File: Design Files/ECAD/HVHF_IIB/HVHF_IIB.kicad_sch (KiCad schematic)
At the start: 70 parts, among them J1 1984963, J2 1984963, J3 731375003, J4 CONSMA002-L, J5 1984963, Q1 PNP, Q2 BFP196E6327HTSA1, T1 BFU590G, T10 BFQ252, T11 BFQ252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

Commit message: fixed orientation error T4,T10-T12
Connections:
- net GND: now also T10.2 (C), T11.2 (C), T4.2 (C); no longer T10.1 (E), T11.1 (E), T12.1 (E), T4.1 (E)
- net at R21.2, T7.1 (E): now also T11.1 (E); no longer T11.2 (C)
- net at R12.2, T5.1 (E): now also T4.1 (E); no longer T4.2 (C)
- net at R22.2, T9.1 (E): now also T12.1 (E); no longer T12.2 (C)
- net at R20.2, T6.1 (E): now also T10.1 (E); no longer T10.2 (C)

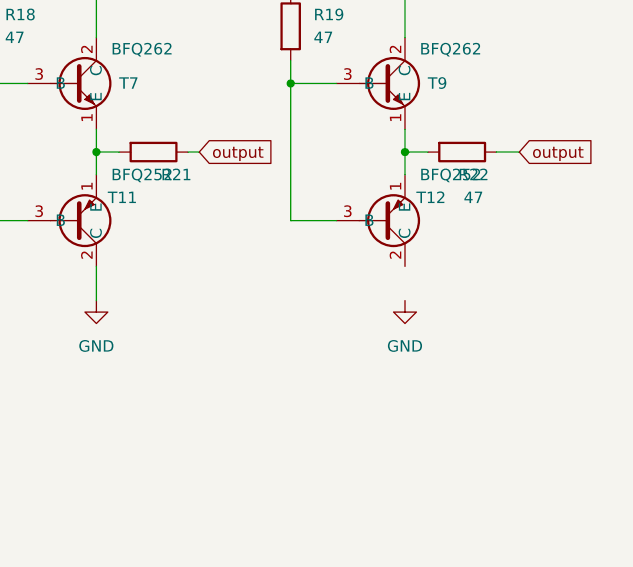
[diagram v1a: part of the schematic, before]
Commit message: fixed unconnected GND power pin
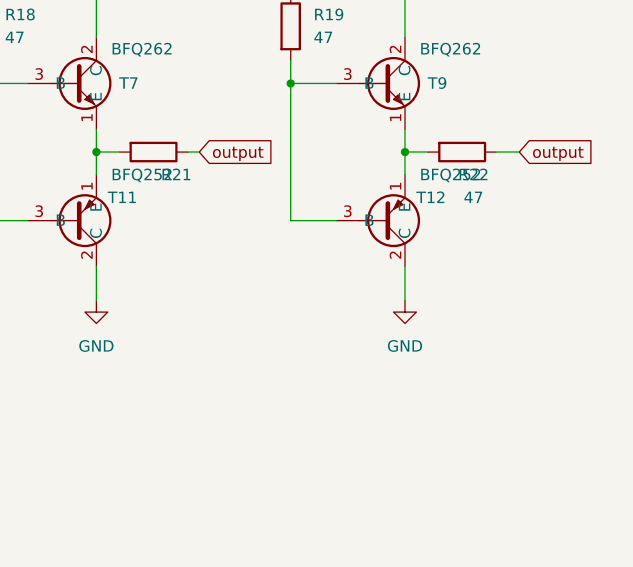
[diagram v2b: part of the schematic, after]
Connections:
- net GND: now also T12.2 (C)
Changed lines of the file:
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@@
+    (stroke (width 0) (type default))
+  )
+  (wire (pts (xy 262.89 154.94) (xy 262.89 158.75))
     (stroke (width 0) (type default))
   )

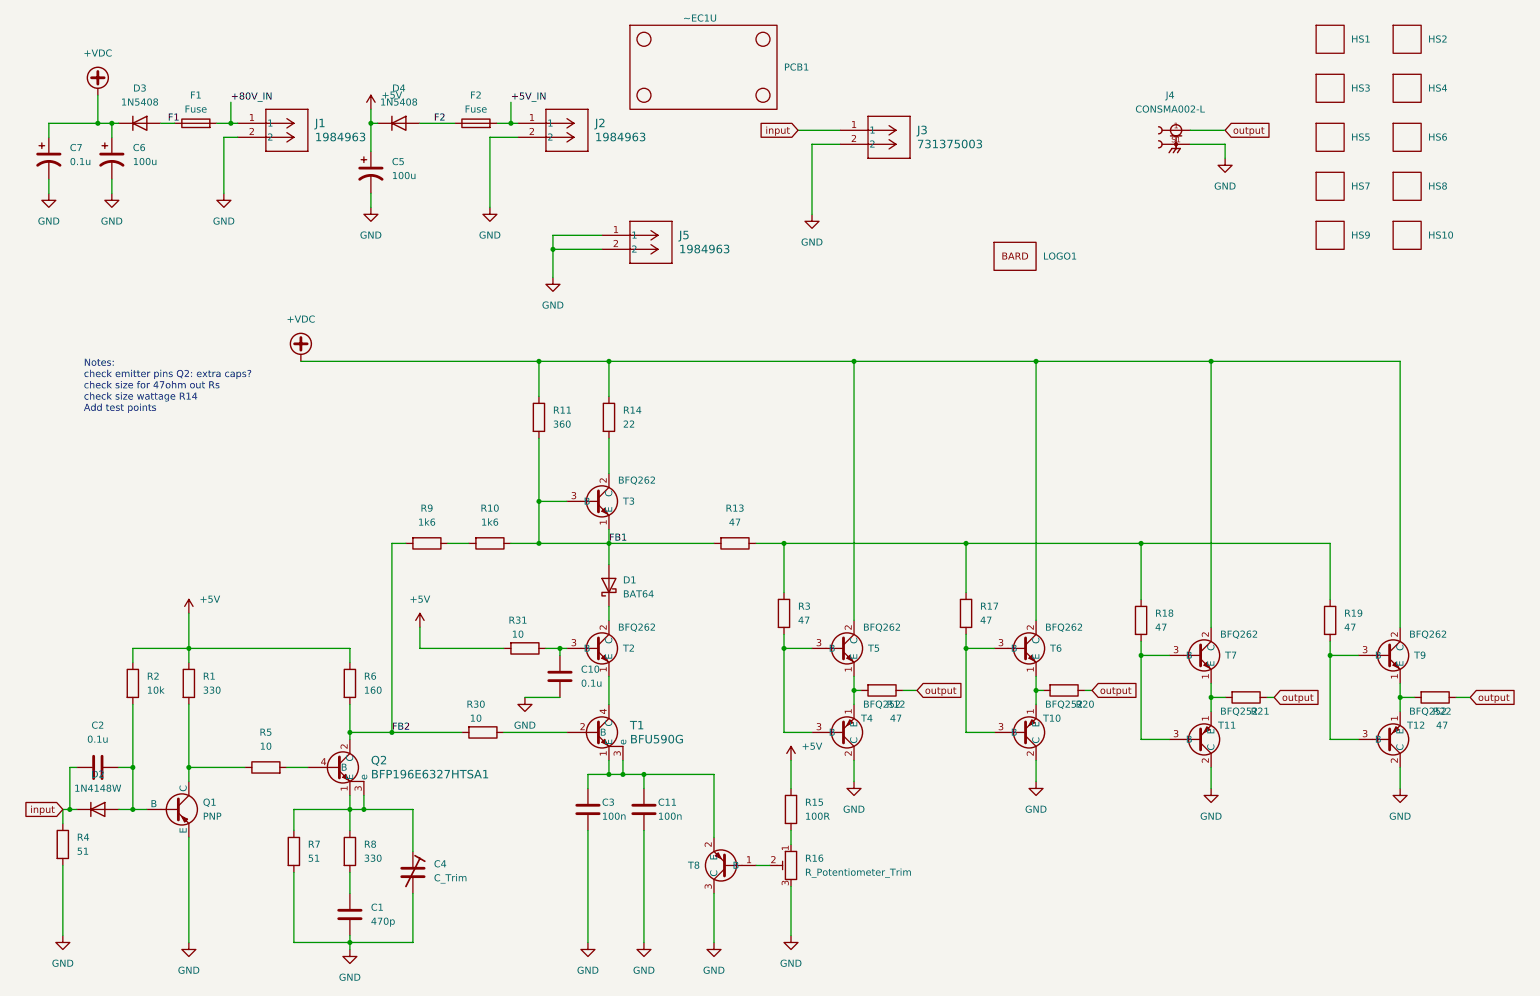
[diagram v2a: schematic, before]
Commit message: fixes, adds, silk
fixed Q1 rotation
adds LED
adds GND
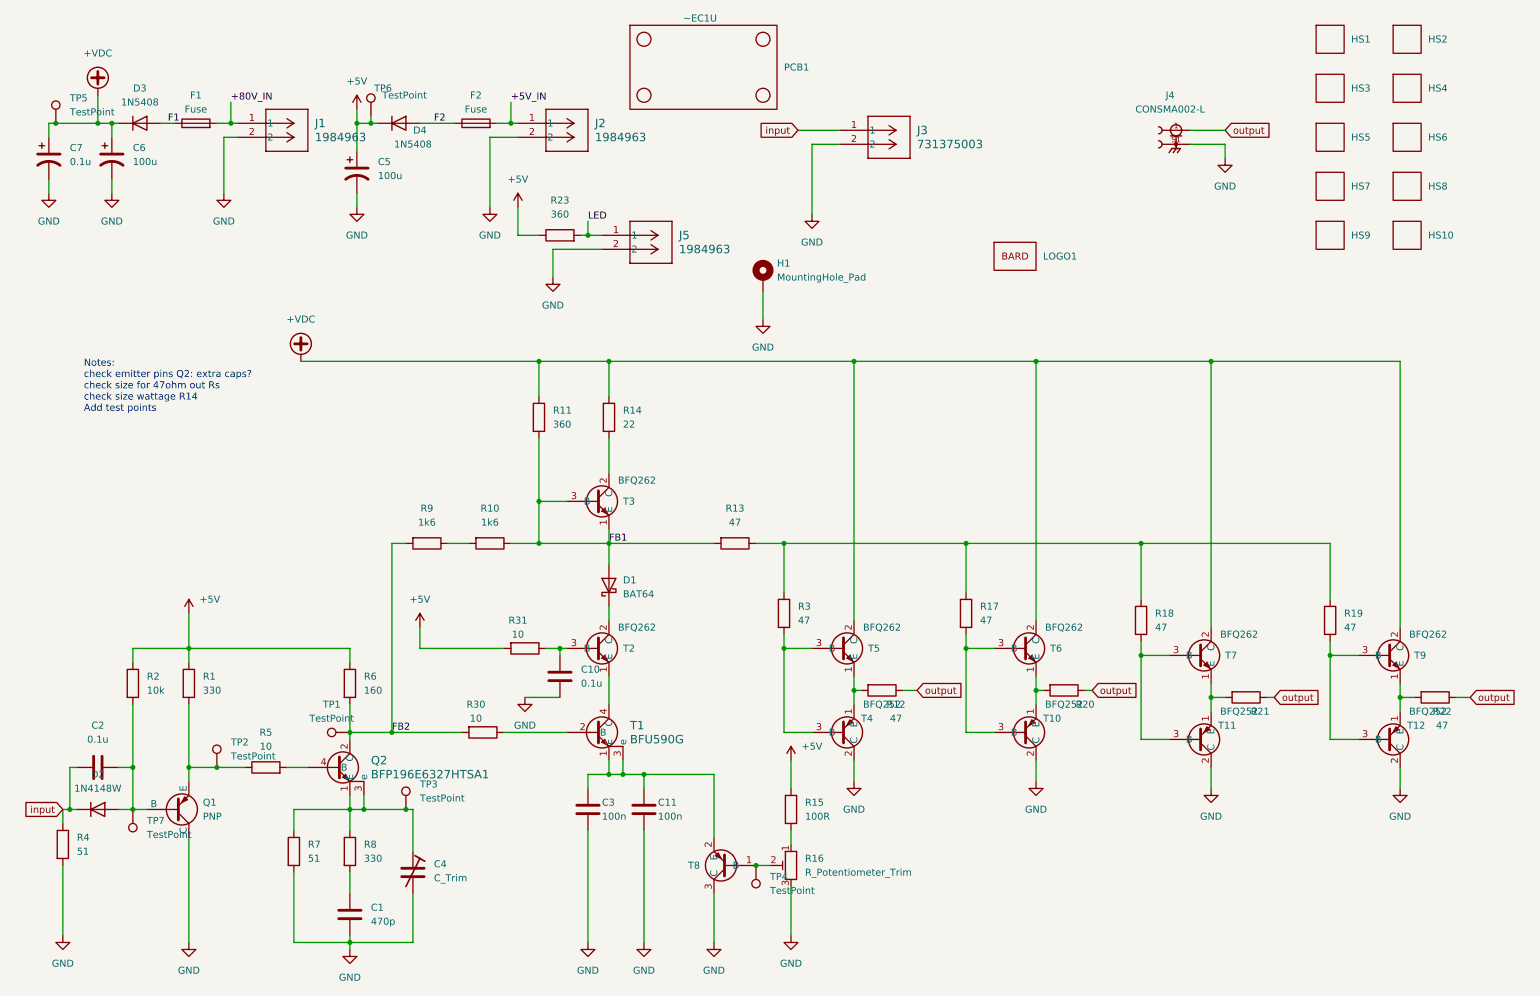
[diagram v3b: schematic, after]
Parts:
- added H1: MountingHole_Pad, Connector_Pin:Pin_D1.4mm_L8.5mm_W2.8mm_FlatFork, symbol Mechanical:MountingHole_Pad
- added R23: 360, Resistor_SMD:R_0805_2012Metric_Pad1.20x1.40mm_HandSolder, symbol Device:R
- added TP1, TP2, TP3, TP4, TP5, TP6, TP7: TestPoint, TestPoint:TestPoint_Pad_D1.0mm, symbol Connector:TestPoint
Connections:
- net +5V: now also R23.1, TP6.1
- net +VDC: now also TP5.1
- net FB2: now also TP1.1
- net GND: now also Q1.1 (C), H1.1; no longer J5.1, Q1.3 (E)
- net at C2.2, D2.2 (A), Q1.2 (B)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: now also TP7.1
- net at R1.2, R5.1: now also Q1.3 (E), TP2.1; no longer Q1.1 (C)
- net at C4.1, Q2.1 (E), Q2.3 (e)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: now also TP3.1
- net at R16.2, T8.1 (B): now also TP4.1
- new net LED: J5.1, R23.2
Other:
- moved on the sheet: C5

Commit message: trace length matching
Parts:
- D2: renamed from D1; footprint Library:CR_BAS70-02V_INF-L -> Library:SOT-23_ONS
- renumbered D2 to D1
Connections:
- net FB1: now also D2.1 (A); no longer D2.2 (A)
- net at T2.2 (C): now also D2.3 (K); no longer D2.1 (K)
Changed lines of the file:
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@@
   (symbol (lib_id "Device:D_Schottky") (at 119.38 121.92 90) (unit 1)
     (in_bom yes) (on_board yes) (dnp no) (fields_autoplaced)
-    (property "Reference" "D1" (at 121.92 120.9675 90)
+    (property "Reference" "D2" (at 121.92 120.9675 90)
       (effects (font (size 1.27 1.27)) (justify right))
     )
@@
       (effects (font (size 1.27 1.27)) (justify right))
     )
-    (property "Footprint" "Library:CR_BAS70-02V_INF-L" (at 119.38 121.92 0)
+    (property "Footprint" "Library:SOT-23_ONS" (at 121.92 121.92 0)
       (effects (font (size 1.27 1.27)) hide)
     )
@@
       (effects (font (size 1.27 1.27)) hide)
     )
-    (pin "1")
-    (pin "2")
-    (instances
-      (project "HVHF_IIB"
-        (path "/a4785c7b-64d4-4462-915b-801e602c6997"
-          (reference "D1") (unit 1)
+    (pin "3")
+    (pin "1")
+    (instances
+      (project "HVHF_IIB"
+        (path "/a4785c7b-64d4-4462-915b-801e602c6997"
+          (reference "D2") (unit 1)
         )
       )
@@
   )
   (symbol (lib_id "Diode:1N4148W") (at 26.67 162.56 0) (unit 1)
-    (in_bom yes) (on_board yes) (dnp no) (fields_autoplaced)
-    (property "Reference" "D2" (at 26.67 156.21 0)
+    (in_bom yes) (on_board yes) (dnp no)
+    (property "Reference" "D1" (at 26.67 166.37 0)
       (effects (font (size 1.27 1.27)))
     )
@@
       (project "HVHF_IIB"
         (path "/a4785c7b-64d4-4462-915b-801e602c6997"
-          (reference "D2") (unit 1)
-        )
-      )
+          (reference "D1") (unit 1)
+        )
+      )

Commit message: Post DR
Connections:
- net FB1: no longer R11.2, T3.3 (B)
- net at D2.3 (K), T2.2 (C): now also R11.2, T3.3 (B)
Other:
- note added: "Notes: check emitter pins Q2: extra caps? check size for 47ohm out Rs check size wattage R14 Why two FB resistors?"
- note removed: "Notes: check emitter pins Q2: extra caps? check size for 47ohm out Rs check size wattage R14 Add test points"
- moved on the sheet: D2
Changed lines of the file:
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@@
   (junction (at 163.83 140.97) (diameter 0) (color 0 0 0 0)
   )
-  (junction (at 106.68 106.68) (diameter 0) (color 0 0 0 0)
-  )
   (junction (at 151.13 133.35) (diameter 0) (color 0 0 0 0)
   )
   (junction (at 43.18 154.94) (diameter 0) (color 0 0 0 0)
   )
+  (junction (at 119.38 114.3) (diameter 0) (color 0 0 0 0)
+  )
   (junction (at 151.13 114.3) (diameter 0) (color 0 0 0 0)
   )
   (junction (at 146.05 172.72) (diameter 0) (color 0 0 0 0)
   )
+  (junction (at 106.68 106.68) (diameter 0) (color 0 0 0 0)
+  )
   (junction (at 121.92 156.21) (diameter 0) (color 0 0 0 0)
   )
@@
   (junction (at 21.59 162.56) (diameter 0) (color 0 0 0 0)
   )
+  (junction (at 119.38 127) (diameter 0) (color 0 0 0 0)
+  )
   (junction (at 76.2 38.1) (diameter 0) (color 0 0 0 0)
   )
   (junction (at 262.89 142.24) (diameter 0) (color 0 0 0 0)
   )
-  (junction (at 119.38 114.3) (diameter 0) (color 0 0 0 0)
-  )
   (junction (at 33.02 154.94) (diameter 0) (color 0 0 0 0)
   )
@@
   (junction (at 215.9 114.3) (diameter 0) (color 0 0 0 0)
   )
-  (junction (at 106.68 114.3) (diameter 0) (color 0 0 0 0)
-  )
   (junction (at 29.21 38.1) (diameter 0) (color 0 0 0 0)
   )
@@
     (stroke (width 0) (type default))
   )
+  (wire (pts (xy 106.68 106.68) (xy 111.76 106.68))
+    (stroke (width 0) (type default))
+  )
   (wire (pts (xy 101.6 38.1) (xy 102.87 38.1))
     (stroke (width 0) (type default))
@@
     (stroke (width 0) (type default))
   )
+  (wire (pts (xy 119.38 111.76) (xy 119.38 114.3))
+    (stroke (width 0) (type default))
+  )
   (wire (pts (xy 29.21 38.1) (xy 29.21 40.64))
     (stroke (width 0) (type default))
@@
     (stroke (width 0) (type default))
   )
+  (wire (pts (xy 119.38 114.3) (xy 119.38 116.84))
+    (stroke (width 0) (type default))
+  )
   (wire (pts (xy 119.38 95.25) (xy 119.38 101.6))
     (stroke (width 0) (type default))
@@
     (stroke (width 0) (type default))
   )
+  (wire (pts (xy 106.68 95.25) (xy 106.68 106.68))
+    (stroke (width 0) (type default))
+  )
   (wire (pts (xy 215.9 149.86) (xy 220.98 149.86))
     (stroke (width 0) (type default))
@@
     (stroke (width 0) (type default))
   )
+  (wire (pts (xy 106.68 127) (xy 119.38 127))
+    (stroke (width 0) (type default))
+  )
   (wire (pts (xy 17.78 48.26) (xy 17.78 50.8))
     (stroke (width 0) (type default))
@@
     (stroke (width 0) (type default))
   )
-  (wire (pts (xy 106.68 114.3) (xy 119.38 114.3))
-    (stroke (width 0) (type default))
-  )
   (wire (pts (xy 72.39 160.02) (xy 72.39 162.56))
     (stroke (width 0) (type default))
@@
     (stroke (width 0) (type default))
   )
+  (wire (pts (xy 106.68 106.68) (xy 106.68 127))
+    (stroke (width 0) (type default))
+  )
   (wire (pts (xy 30.48 154.94) (xy 33.02 154.94))
     (stroke (width 0) (type default))
@@
     (stroke (width 0) (type default))
   )
+  (wire (pts (xy 119.38 114.3) (xy 138.43 114.3))
+    (stroke (width 0) (type default))
+  )
   (wire (pts (xy 43.18 143.51) (xy 43.18 154.94))
     (stroke (width 0) (type default))
@@
     (stroke (width 0) (type default))
   )
-  (wire (pts (xy 119.38 125.73) (xy 119.38 128.27))
+  (wire (pts (xy 115.57 156.21) (xy 115.57 158.75))
     (stroke (width 0) (type default))
   )
-  (wire (pts (xy 115.57 156.21) (xy 115.57 158.75))
+  (wire (pts (xy 119.38 124.46) (xy 119.38 127))
     (stroke (width 0) (type default))
   )
@@
     (stroke (width 0) (type default))
   )
-  (wire (pts (xy 119.38 114.3) (xy 138.43 114.3))
+  (wire (pts (xy 101.6 114.3) (xy 119.38 114.3))
     (stroke (width 0) (type default))
   )
@@
     (stroke (width 0) (type default))
   )
-  (wire (pts (xy 101.6 114.3) (xy 106.68 114.3))
-    (stroke (width 0) (type default))
-  )
   (wire (pts (xy 119.38 153.67) (xy 119.38 156.21))
     (stroke (width 0) (type default))
@@
     (stroke (width 0) (type default))
   )
-  (wire (pts (xy 119.38 111.76) (xy 119.38 114.3))
-    (stroke (width 0) (type default))
-  )
   (wire (pts (xy 224.79 41.91) (xy 231.14 41.91))
     (stroke (width 0) (type default))
@@
     (stroke (width 0) (type default))
   )
-  (wire (pts (xy 106.68 95.25) (xy 106.68 106.68))
-    (stroke (width 0) (type default))
-  )
   (wire (pts (xy 106.68 81.28) (xy 106.68 87.63))
     (stroke (width 0) (type default))
@@
     (stroke (width 0) (type default))
   )
-  (wire (pts (xy 106.68 106.68) (xy 111.76 106.68))
+  (wire (pts (xy 85.09 129.54) (xy 85.09 133.35))
     (stroke (width 0) (type default))
   )
-  (wire (pts (xy 85.09 129.54) (xy 85.09 133.35))
+  (wire (pts (xy 119.38 127) (xy 119.38 128.27))
     (stroke (width 0) (type default))
   )
@@
     (stroke (width 0) (type default))
   )
-  (wire (pts (xy 119.38 114.3) (xy 119.38 118.11))
-    (stroke (width 0) (type default))
-  )
   (wire (pts (xy 163.83 81.28) (xy 163.83 128.27))
     (stroke (width 0) (type default))
   )
-  (wire (pts (xy 106.68 106.68) (xy 106.68 114.3))
-    (stroke (width 0) (type default))
-  )
   (wire (pts (xy 106.68 81.28) (xy 119.38 81.28))
     (stroke (width 0) (type default))
@@
     (stroke (width 0) (type default))
   )
-  (text "Notes:\ncheck emitter pins Q2: extra caps?\ncheck size for 47ohm out Rs\ncheck size wattage R14\nAdd test points\n\n"
+  (text "Notes:\ncheck emitter pins Q2: extra caps?\ncheck size for 47ohm out Rs\ncheck size wattage R14\nWhy two FB resistors?\n\n\n"
     (at 24.13 92.71 0)
     (effects (font (size 1.27 1.27)) (justify left bottom))
@@
     )
   )
-  (netclass_flag "" (length 2.54) (shape round) (at 119.38 127 0) (fields_autoplaced)
-    (effects (font (size 1.27 1.27)) (justify left bottom))
-    (property "Netclass" "sig" (at 120.0785 124.46 0)
-      (effects (font (size 1.27 1.27) italic) (justify left))
-    )
-  )
   (netclass_flag "" (length 2.54) (shape round) (at 33.02 154.94 0) (fields_autoplaced)
     (effects (font (size 1.27 1.27)) (justify left bottom))
@@
     )
   )
-  (netclass_flag "" (length 2.54) (shape round) (at 119.38 116.84 0) (fields_autoplaced)
+  (netclass_flag "" (length 2.54) (shape round) (at 129.54 114.3 0) (fields_autoplaced)
     (effects (font (size 1.27 1.27)) (justify left bottom))
-    (property "Netclass" "sig" (at 120.0785 114.3 0)
+    (property "Netclass" "sig" (at 130.2385 111.76 0)
       (effects (font (size 1.27 1.27) italic) (justify left))
     )
@@
     )
   )
-  (symbol (lib_id "Device:D_Schottky") (at 119.38 121.92 90) (unit 1)
+  (symbol (lib_id "Device:D_Schottky") (at 119.38 120.65 90) (unit 1)
     (in_bom yes) (on_board yes) (dnp no) (fields_autoplaced)
-    (property "Reference" "D2" (at 121.92 120.9675 90)
+    (property "Reference" "D2" (at 121.92 119.6975 90)
       (effects (font (size 1.27 1.27)) (justify right))
     )
-    (property "Value" "BAT64" (at 121.92 123.5075 90)
+    (property "Value" "BAT64" (at 121.92 122.2375 90)
       (effects (font (size 1.27 1.27)) (justify right))
     )
-    (property "Footprint" "Library:SOT-23_ONS" (at 121.92 121.92 0)
+    (property "Footprint" "Library:SOT-23_ONS" (at 121.92 120.65 0)
       (effects (font (size 1.27 1.27)) hide)
     )
-    (property "Datasheet" "~" (at 119.38 121.92 0)
+    (property "Datasheet" "~" (at 119.38 120.65 0)
       (effects (font (size 1.27 1.27)) hide)
     )
@@
       (effects (font (size 1.27 1.27)) (justify left))
     )
-    (property "Value" "BFQ252" (at 233.68 144.78 0)
+    (property "Value" "BFQ252" (at 234.95 149.86 0)
       (effects (font (size 1.27 1.27)))
     )
@@
       (effects (font (size 1.27 1.27)) (justify left))
     )
-    (property "Value" "BFQ252" (at 267.97 144.78 0)
+    (property "Value" "BFQ252" (at 269.24 151.13 0)
       (effects (font (size 1.27 1.27)))
     )
@@
       (effects (font (size 1.27 1.27)) (justify left))
     )
-    (property "Value" "BFQ252" (at 168.91 143.51 0)
+    (property "Value" "BFQ252" (at 171.45 149.86 0)
       (effects (font (size 1.27 1.27)))
     )
@@
       (effects (font (size 1.27 1.27)) (justify left))
     )
-    (property "Value" "BFQ252" (at 201.93 143.51 0)
+    (property "Value" "BFQ252" (at 204.47 148.59 0)
       (effects (font (size 1.27 1.27)))
     )

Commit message: stitching done
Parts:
- R12, R20, R21, R22: footprint Library:RES_3560_TEC -> Library:RES_ALSR05_VIS
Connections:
- net +VDC: now also C7.2; no longer C7.1
- net GND: now also C7.1; no longer C7.2
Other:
- moved on the sheet: C7
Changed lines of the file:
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@@
     )
   )
-  (symbol (lib_id "Device:C_Polarized_US") (at 17.78 44.45 0) (unit 1)
-    (in_bom yes) (on_board yes) (dnp no) (fields_autoplaced)
-    (property "Reference" "C7" (at 21.59 42.545 0)
-      (effects (font (size 1.27 1.27)) (justify left))
-    )
-    (property "Value" "0.1u" (at 21.59 45.085 0)
-      (effects (font (size 1.27 1.27)) (justify left))
+  (symbol (lib_id "Device:C_Polarized_US") (at 17.78 44.45 180) (unit 1)
+    (in_bom yes) (on_board yes) (dnp no) (fields_autoplaced)
+    (property "Reference" "C7" (at 21.59 43.815 0)
+      (effects (font (size 1.27 1.27)) (justify right))
+    )
+    (property "Value" "0.1u" (at 21.59 46.355 0)
+      (effects (font (size 1.27 1.27)) (justify right))
     )
     (property "Footprint" "Capacitor_SMD:C_1206_3216Metric_Pad1.33x1.80mm_HandSolder" (at 17.78 44.45 0)
@@
       (effects (font (size 1.27 1.27)) hide)
     )
+    (pin "1")
     (pin "3")
-    (pin "1")
     (instances
       (project "HVHF_IIB"
@@
       (effects (font (size 1.27 1.27)) hide)
     )
-    (property "Footprint" "Library:RES_3560_TEC" (at 234.95 140.462 90)
+    (property "Footprint" "Library:RES_ALSR05_VIS" (at 234.95 140.462 90)
       (effects (font (size 1.27 1.27)) hide)
     )
@@
       (effects (font (size 1.27 1.27)))
     )
-    (property "Footprint" "Library:RES_3560_TEC" (at 168.91 139.192 90)
+    (property "Footprint" "Library:RES_ALSR05_VIS" (at 168.91 139.192 90)
       (effects (font (size 1.27 1.27)) hide)
     )
@@
       (effects (font (size 1.27 1.27)) hide)
     )
-    (property "Footprint" "Library:RES_3560_TEC" (at 201.93 139.192 90)
+    (property "Footprint" "Library:RES_ALSR05_VIS" (at 201.93 139.192 90)
       (effects (font (size 1.27 1.27)) hide)
     )
@@
       (effects (font (size 1.27 1.27)))
     )
-    (property "Footprint" "Library:RES_3560_TEC" (at 269.24 140.462 90)
-      (effects (font (size 1.27 1.27)) hide)
-    )
+    (property "Footprint" "Library:RES_ALSR05_VIS" (at 269.24 140.462 90)
+      (effects (font (size 1.27 1.27)) hide)
+    )
